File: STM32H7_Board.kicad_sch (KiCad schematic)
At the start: 0 parts

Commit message: Update
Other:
- sheet STM32H7S3I8T6 ports: added FMC_BA0, FMC_BA1, FMC_SDCLK, PD12, PD8_FMC_NBL0, PE11_FMC_SDNWE, PE12_FMC_SDNRAS, PE13_FMC_SDNCAS, PE14_FMC_SDNE0, PE15_FMC_SDCKE0, PF4; removed FMC_A13, FMC_A14, PD12_FMC_NE1, PD8, PD9, PE10, PE11, PE12, PE13, PE14, PE15

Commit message: Update
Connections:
- no-connect marks 17 -> 15
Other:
- removed sheet Camera_Interface
- sheet Interface_Headers ports: added BTB10, BTB11, BTB12, BTB13, BTB14, BTB15, BTB16, BTB17, BTB18, BTB19, BTB31, BTB32, BTB33, BTB34, BTB35, BTB36, BTB37, BTB38, BTB39, BTB40, BTB41, BTB42, BTB43, BTB44, BTB45, BTB46, BTB47, BTB48, BTB49, BTB50, BTB51, BTB52, BTB53, BTB54, BTB55, BTB56, BTB57, BTB58, BTB59, BTB60, BTB7, BTB8, BTB9; removed none
- sheet Power_Management ports: added none; removed INTN, PWRCTRL, RSTN, SCL_STPMIC1, SDA_STPMIC1, WAKEUP
- sheet STM32H7S3I8T6 ports: added PA5_I2S1_CK, PA7_I2S6_SDO, PB10_SPI2_SCK, PB11, PB13_UART5_TX, PB4_I2S1_SDI, PB5_SPI3_MOSI, PB6_LPUART1_TX, PB7_PSSI_RDY, PC10_SPI3_SCK, PC11_SPI3_MISO, PC6_PSSI_D0, PC7_PSSI_D1, PC8_PSSI_D2, PC9_PSSI_D3, PD10_PSSI_D4, PD11_PSSI_D6, PD13_FMC_INT, PD14_PSSI_D7, PD3_PSSI_D5, PD4_PSSI_DE, PD9_FMC_SDCLK, PF8_PSSI_PDCK, PO0, PO4, PP0, PP1, PP2, PP3; removed DCMIPP_D0, DCMIPP_D1, DCMIPP_D2, DCMIPP_D3, DCMIPP_D4, DCMIPP_D5, DCMIPP_D6, DCMIPP_D7, DCMIPP_HSYNC, DCMIPP_VSYNC, FMC_SDCLK, PA5, PA7_FMC_INT, PB10_I2C2_SCL, PB11_I2C2_SDA, PB13_SPI2_SCK, PB5_I2S6_SDO, PB6_UART5_TX, PB7, PC10_I2S3_CK, PC11_I2S3_SDI, PD13, PF8_DCMIPP_PIXCLK, PO0_XSPIM_P1_NCS1, PO4_XSPIM_P1_CLK, PP0_XSPIM_P1_IO0, PP1_XSPIM_P1_IO1, PP2_XSPIM_P1_IO2, PP3_XSPIM_P1_IO3

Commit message: Update
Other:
- sheet LCD_Interface ports: added FMC_A9, FMC_NE3; removed FMC_A0, FMC_NE1
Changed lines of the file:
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@@
 		)
 	)
-	(label "FMC_A0"
+	(label "FMC_A9"
 		(at 119.38 237.49 0)
 		(fields_autoplaced yes)
@@
 		)
 	)
-	(label "FMC_NOE"
-		(at 119.38 242.57 0)
-		(fields_autoplaced yes)
-		(effects
-			(font
-				(size 1.27 1.27)
-			)
-			(justify left bottom)
-		)
-	)
 	(label "FMC_A2"
 		(at 189.23 33.02 180)
@@
 		)
 	)
-	(label "FMC_NE1"
-		(at 119.38 245.11 0)
-		(fields_autoplaced yes)
-		(effects
-			(font
-				(size 1.27 1.27)
-			)
-			(justify left bottom)
-		)
-	)
 	(label "FMC_A4"
 		(at 189.23 38.1 180)
@@
 	(label "FMC_D0"
 		(at 119.38 193.04 0)
-		(fields_autoplaced yes)
-		(effects
-			(font
-				(size 1.27 1.27)
-			)
-			(justify left bottom)
-		)
-	)
-	(label "FMC_NWE"
-		(at 119.38 240.03 0)
 		(fields_autoplaced yes)
 		(effects
@@
 		)
 		(pin "RST_PWR" input
-			(at 317.5 246.38 180)
+			(at 317.5 245.11 180)
 			(effects
 				(font
@@
 			)
 		)
-		(pin "FMC_A0" bidirectional
-			(at 119.38 237.49 0)
-			(effects
-				(font
-					(size 1.27 1.27)
-				)
-				(justify right)
-			)
-		)
 		(pin "FMC_NWE" bidirectional
 			(at 119.38 240.03 0)
@@
 			)
 		)
-		(pin "FMC_NE1" bidirectional
-			(at 119.38 245.11 0)
-			(effects
-				(font
-					(size 1.27 1.27)
-				)
-				(justify right)
-			)
-		)
 		(pin "LCD_RESET" bidirectional
 			(at 119.38 264.16 0)
@@
 			(effects
 				(font
+					(size 1.27 1.27)
+				)
+				(justify right)
+			)
+		)
+		(pin "FMC_NE3" bidirectional
+			(at 119.38 245.11 0)
+			(effects
+				(font
+					(size 1.27 1.27)
+				)
+				(justify right)
+			)
+		)
+		(pin "FMC_A9" bidirectional
+			(at 119.38 237.49 0)
+			(effects
+				(font

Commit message: Update
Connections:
- no-connect marks 15 -> 12

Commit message: Update
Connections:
- no-connect marks 12 -> 25
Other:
- sheet Interface_Headers ports: added none; removed USR_BTN
- company: (none) -> Peter Hancak
- title: (none) -> STM32H7S3 Board

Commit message: Pin typo fix
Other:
- sheet STM32H7S3I8T6 ports: added PA4_I2S1_WS; removed PA4_I2S3_WS
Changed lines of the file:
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@@
-			)
-		)
-		(pin "PA4_I2S3_WS" output
-			(at 245.11 90.17 0)
-			(effects
-				(font
-					(size 1.27 1.27)
-				)
-				(justify right)
 			)
 		)
@@
 			(effects
 				(font
+					(size 1.27 1.27)
+				)
+				(justify right)
+			)
+		)
+		(pin "PA4_I2S1_WS" output
+			(at 245.11 90.17 0)
+			(effects
+				(font

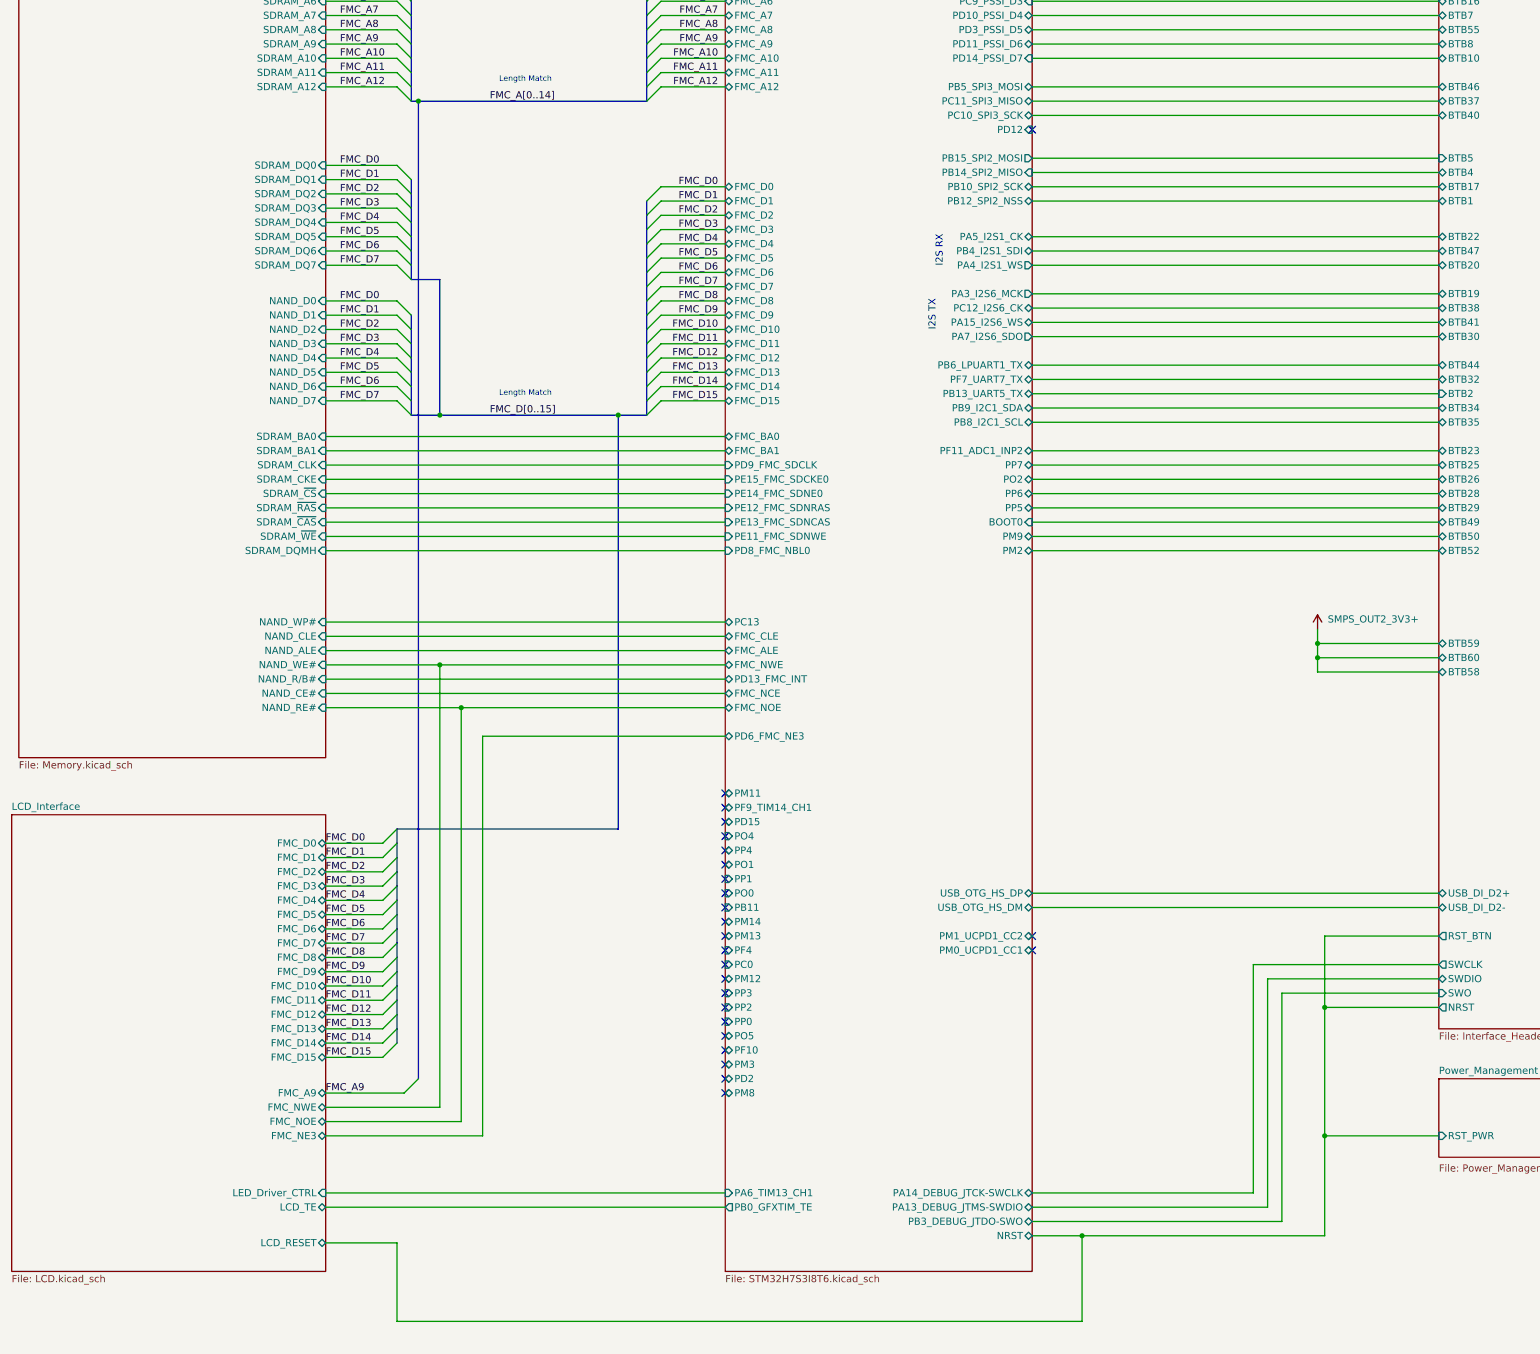
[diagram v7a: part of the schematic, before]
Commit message: Added I2C to the LCD interface
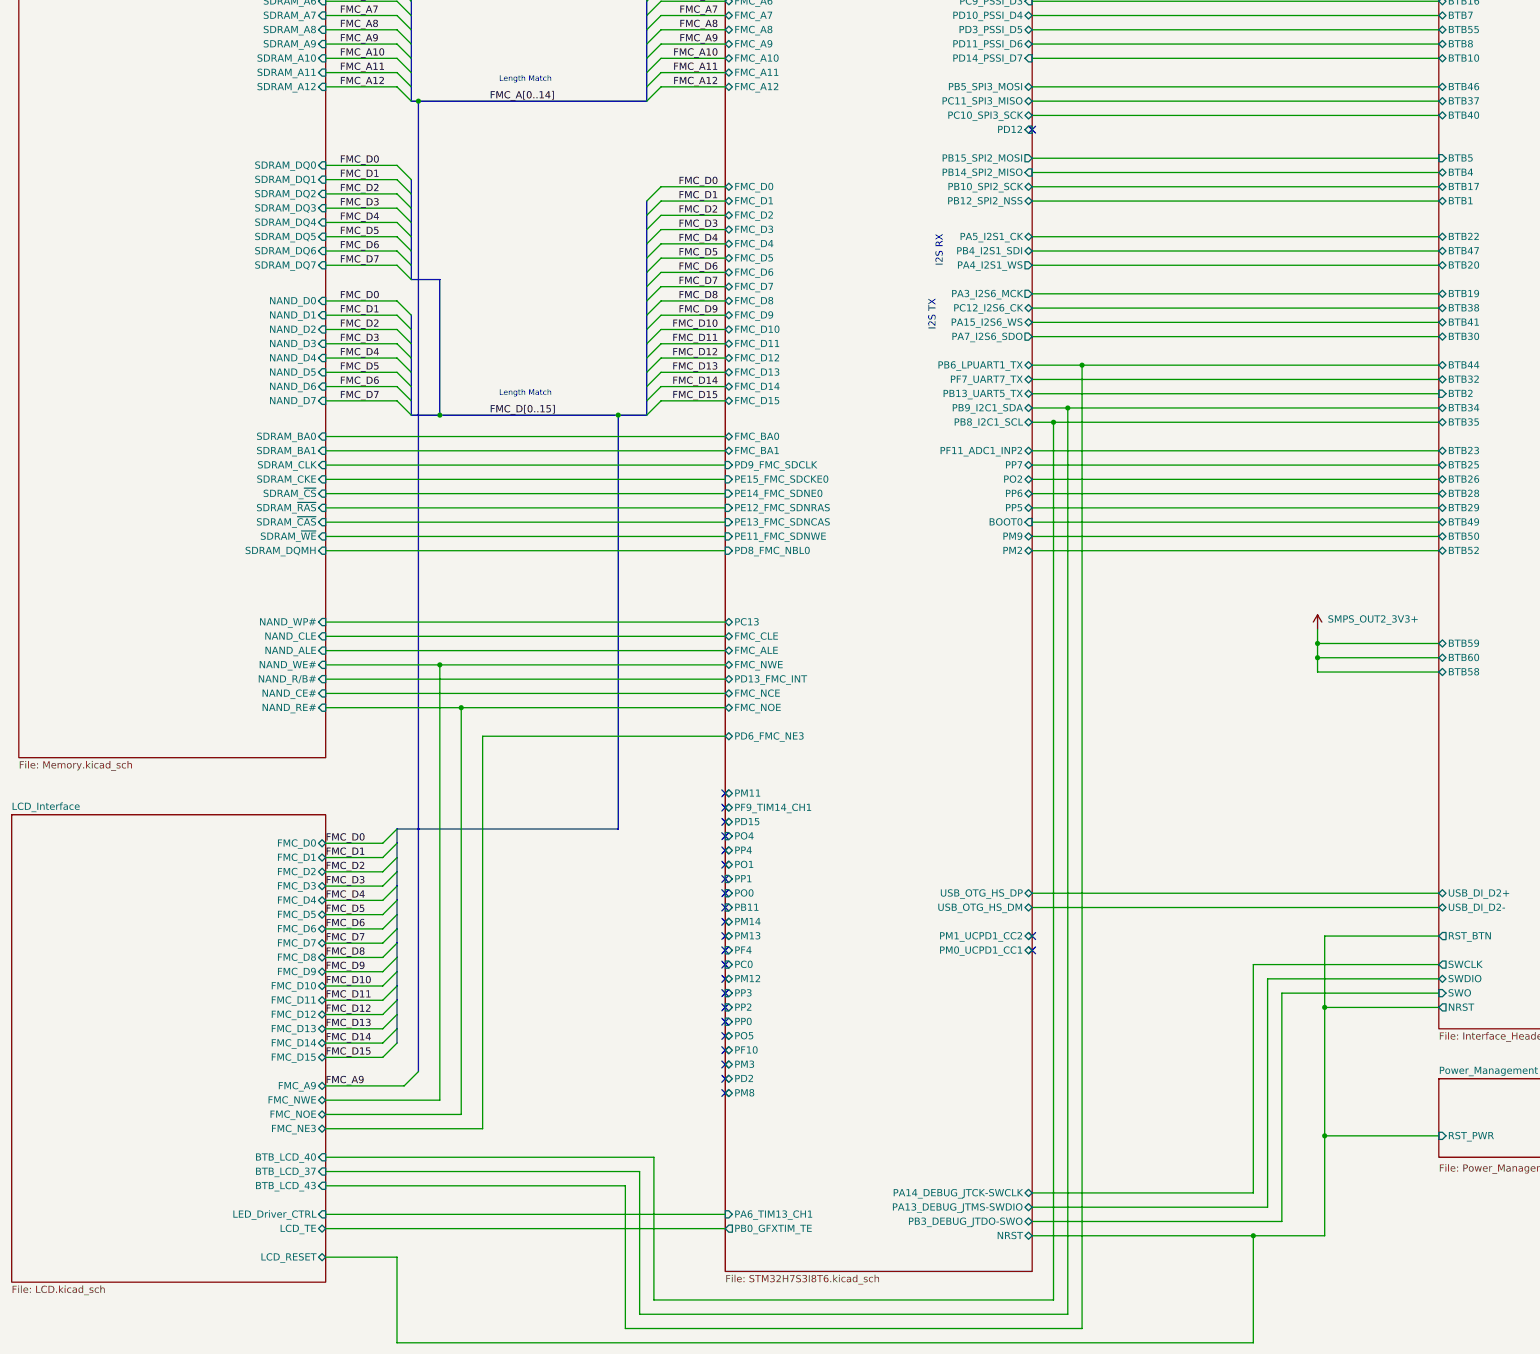
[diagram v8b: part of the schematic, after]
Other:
- sheet LCD_Interface ports: added BTB_LCD_37, BTB_LCD_40, BTB_LCD_43; removed none
